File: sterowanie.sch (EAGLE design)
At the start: 8 parts

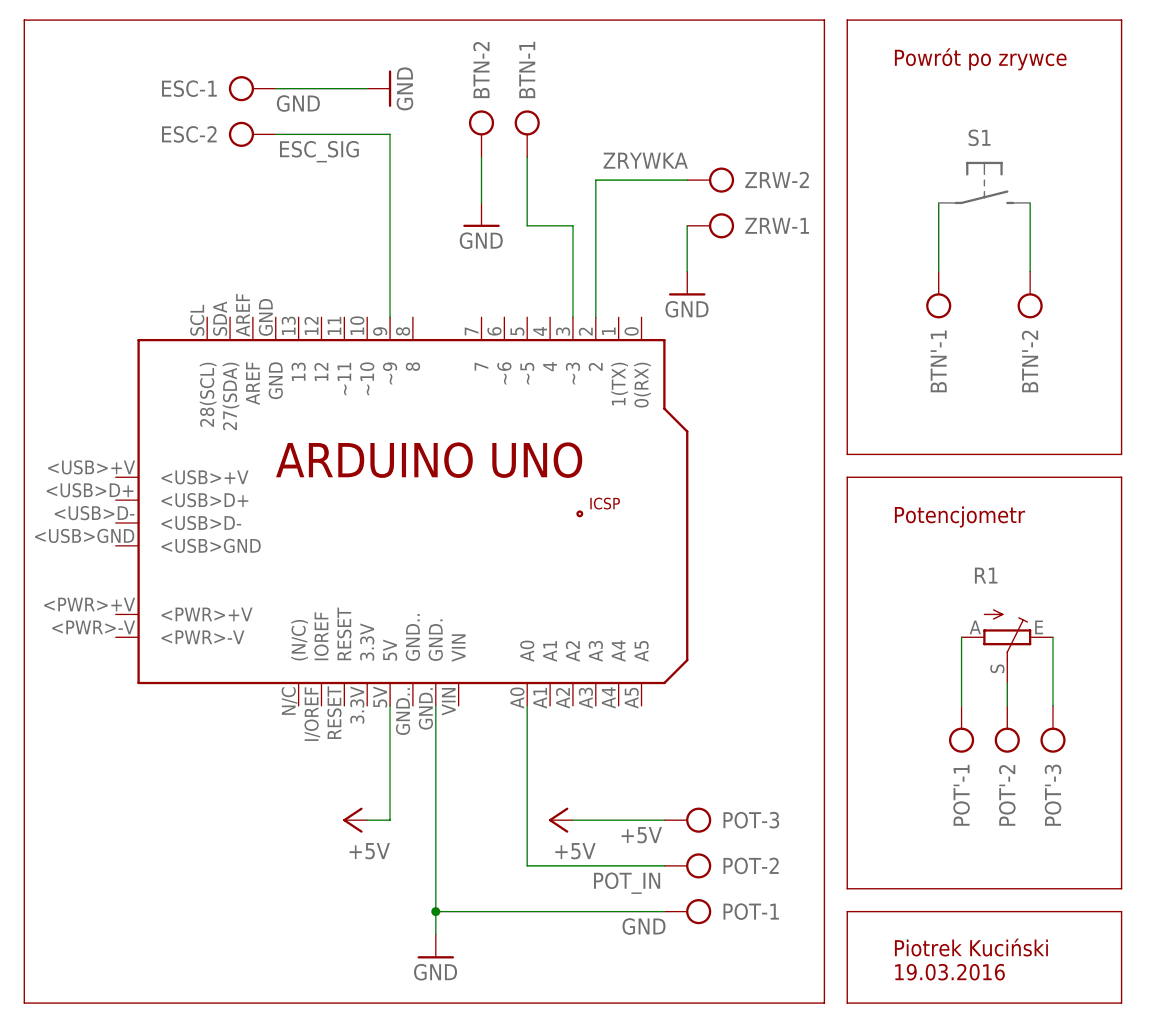
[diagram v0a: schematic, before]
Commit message: poprawiony schemat, dodane PCB jako shield do Arduino
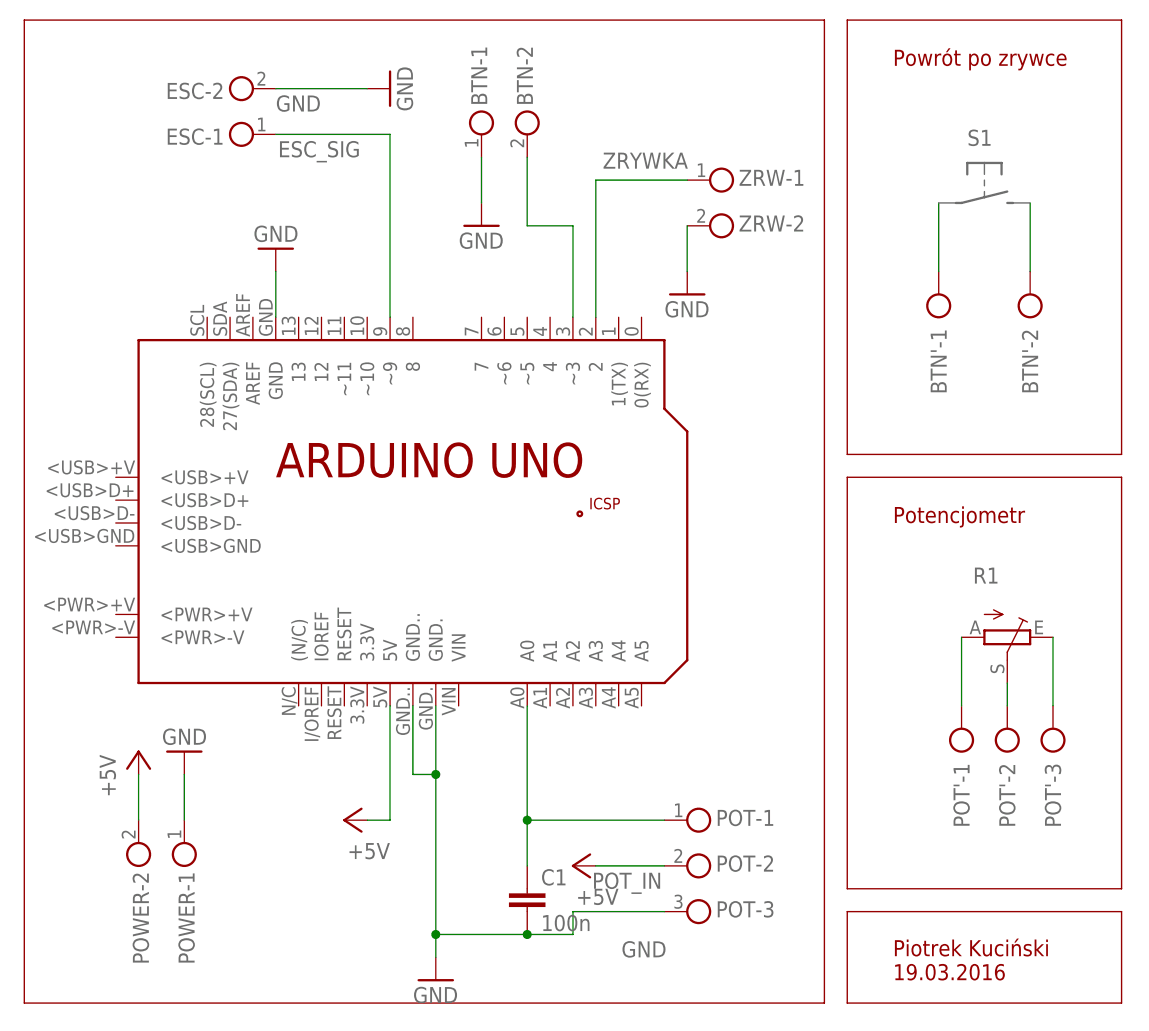
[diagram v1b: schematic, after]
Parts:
- added C1: 100n, rcl:C-EUC1206
- added POWER: (no value), con-ria-59:AKL59-02
- BTN, ESC, ZRW: device con-ptr500:AK300/2 -> con-ria-59:AKL59-02
- POT: device con-ptr500:AK300/3 -> con-ria-59:AKL59-03
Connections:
- net +5V: now also POT-2.1, POWER-2.1; no longer POT-3.KL
- net ESC_SIG: now also ESC-1.1; no longer ESC-2.KL
- net GND: now also BTN-1.1, C1.2, ESC-2.1, PCB1.GND, PCB1.GND.., POT-3.1, POWER-1.1, ZRW-2.1; no longer BTN-2.KL, ESC-1.KL, POT-1.KL, ZRW-1.KL
- net N$1: now also BTN-2.1; no longer BTN-1.KL
- net POT_IN: now also C1.1, POT-1.1; no longer POT-2.KL
- net ZRYWKA: now also ZRW-1.1; no longer ZRW-2.KL
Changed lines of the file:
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@@
 <part name="PCB1" library="E14_Arduino_revB" deviceset="ARDUINO_UNO" device=""/>
 <part name="S1" library="switch-omron" deviceset="D-TS" device=""/>
-<part name="ZRW" library="con-ptr500" deviceset="AK300/2" device=""/>
-<part name="POT" library="con-ptr500" deviceset="AK300/3" device=""/>
-<part name="ESC" library="con-ptr500" deviceset="AK300/2" device=""/>
 <part name="P+1" library="supply1" deviceset="+5V" device=""/>
 <part name="GND1" library="supply1" deviceset="GND" device=""/>
@@
 <part name="GND3" library="supply1" deviceset="GND" device=""/>
 <part name="GND4" library="supply1" deviceset="GND" device=""/>
-<part name="BTN" library="con-ptr500" deviceset="AK300/2" device=""/>
 <part name="BTN'" library="con-ptr500" deviceset="AK300/2" device=""/>
 <part name="POT'" library="con-ptr500" deviceset="AK300/3" device=""/>
 <part name="R1" library="pot" deviceset="TRIM_EU-" device="B90P"/>
+<part name="P+3" library="supply1" deviceset="+5V" device=""/>
+<part name="GND5" library="supply1" deviceset="GND" device=""/>
+<part name="C1" library="rcl" deviceset="C-EU" device="C1206" value="100n"/>
+<part name="POT" library="con-ria-59" deviceset="AKL59-03" device=""/>
+<part name="POWER" library="con-ria-59" deviceset="AKL59-02" device=""/>
+<part name="BTN" library="con-ria-59" deviceset="AKL59-02" device=""/>
+<part name="ESC" library="con-ria-59" deviceset="AKL59-02" device=""/>
+<part name="ZRW" library="con-ria-59" deviceset="AKL59-02" device=""/>
+<part name="GND6" library="supply1" deviceset="GND" device=""/>
 </parts>
 <sheets>
@@
 <instance part="PCB1" gate="G$1" x="76.2" y="43.18"/>
 <instance part="S1" gate="G$1" x="139.7" y="76.2" rot="R270"/>
-<instance part="ZRW" gate="-1" x="111.76" y="73.66" rot="R180"/>
-<instance part="ZRW" gate="-2" x="111.76" y="78.74" rot="R180"/>
-<instance part="POT" gate="-1" x="109.22" y="-2.54" rot="R180"/>
-<instance part="POT" gate="-2" x="109.22" y="2.54" rot="R180"/>
-<instance part="POT" gate="-3" x="109.22" y="7.62" rot="R180"/>
-<instance part="ESC" gate="-1" x="55.88" y="88.9" smashed="yes">
-<attribute name="NAME" x="54.61" y="89.789" size="1.778" layer="95" rot="R180"/>
-</instance>
-<instance part="ESC" gate="-2" x="55.88" y="83.82" smashed="yes">
-<attribute name="NAME" x="54.61" y="84.709" size="1.778" layer="95" rot="R180"/>
-<attribute name="VALUE" x="52.07" y="80.137" size="1.778" layer="96"/>
-</instance>
 <instance part="P+1" gate="1" x="68.58" y="7.62" rot="R90"/>
-<instance part="GND1" gate="1" x="78.74" y="-7.62"/>
-<instance part="P+2" gate="1" x="91.44" y="7.62" rot="R90"/>
+<instance part="GND1" gate="1" x="78.74" y="-10.16"/>
+<instance part="P+2" gate="1" x="93.98" y="2.54" rot="R90"/>
 <instance part="GND2" gate="1" x="73.66" y="88.9" rot="R90"/>
 <instance part="GND3" gate="1" x="106.68" y="66.04"/>
 <instance part="GND4" gate="1" x="83.82" y="73.66"/>
-<instance part="BTN" gate="-1" x="88.9" y="86.36" rot="R270"/>
-<instance part="BTN" gate="-2" x="83.82" y="86.36" rot="R270"/>
 <instance part="BTN'" gate="-1" x="134.62" y="63.5" rot="R90"/>
 <instance part="BTN'" gate="-2" x="144.78" y="63.5" rot="R90"/>
@@
 <instance part="POT'" gate="-3" x="147.32" y="15.24" rot="R90"/>
 <instance part="R1" gate="1" x="142.24" y="27.94" rot="R270"/>
+<instance part="P+3" gate="1" x="45.72" y="15.24"/>
+<instance part="GND5" gate="1" x="50.8" y="15.24" rot="R180"/>
+<instance part="C1" gate="G$1" x="88.9" y="0"/>
+<instance part="POT" gate="-1" x="104.14" y="7.62"/>
+<instance part="POT" gate="-2" x="104.14" y="2.54"/>
+<instance part="POT" gate="-3" x="104.14" y="-2.54"/>
+<instance part="POWER" gate="-1" x="50.8" y="7.62" rot="R270"/>
+<instance part="POWER" gate="-2" x="45.72" y="7.62" rot="R270"/>
+<instance part="BTN" gate="-1" x="83.82" y="81.28" rot="R90"/>
+<instance part="BTN" gate="-2" x="88.9" y="81.28" rot="R90"/>
+<instance part="ESC" gate="-1" x="60.96" y="83.82" rot="R180"/>
+<instance part="ESC" gate="-2" x="60.96" y="88.9" rot="R180"/>
+<instance part="ZRW" gate="-1" x="106.68" y="78.74"/>
+<instance part="ZRW" gate="-2" x="106.68" y="73.66"/>
+<instance part="GND6" gate="1" x="60.96" y="71.12" rot="R180"/>
 </instances>
 <busses>
@@
 </segment>
 <segment>
-<pinref part="POT" gate="-3" pin="KL"/>
+<pinref part="P+3" gate="1" pin="+5V"/>
+<wire x1="45.72" y1="7.62" x2="45.72" y2="12.7" width="0.1524" layer="91"/>
+<pinref part="POWER" gate="-2" pin="1"/>
+</segment>
+<segment>
 <pinref part="P+2" gate="1" pin="+5V"/>
-<wire x1="93.98" y1="7.62" x2="104.14" y2="7.62" width="0.1524" layer="91"/>
-<label x="103.886" y="6.858" size="1.778" layer="95" rot="R180"/>
+<pinref part="POT" gate="-2" pin="1"/>
+<wire x1="96.52" y1="2.54" x2="104.14" y2="2.54" width="0.1524" layer="91"/>
 </segment>
 </net>
@@
 <pinref part="PCB1" gate="G$1" pin="GND."/>
 <pinref part="GND1" gate="1" pin="GND"/>
-<wire x1="78.74" y1="20.32" x2="78.74" y2="-2.54" width="0.1524" layer="91"/>
-<pinref part="POT" gate="-1" pin="KL"/>
-<wire x1="78.74" y1="-2.54" x2="78.74" y2="-5.08" width="0.1524" layer="91"/>
-<wire x1="104.14" y1="-2.54" x2="78.74" y2="-2.54" width="0.1524" layer="91"/>
-<junction x="78.74" y="-2.54"/>
-<label x="104.394" y="-3.302" size="1.778" layer="95" rot="R180"/>
+<wire x1="78.74" y1="20.32" x2="78.74" y2="12.7" width="0.1524" layer="91"/>
+<wire x1="78.74" y1="12.7" x2="78.74" y2="-5.08" width="0.1524" layer="91"/>
+<wire x1="78.74" y1="-5.08" x2="78.74" y2="-7.62" width="0.1524" layer="91"/>
+<junction x="78.74" y="-5.08"/>
+<label x="104.394" y="-5.842" size="1.778" layer="95" rot="R180"/>
+<pinref part="C1" gate="G$1" pin="2"/>
+<wire x1="88.9" y1="-5.08" x2="78.74" y2="-5.08" width="0.1524" layer="91"/>
+<wire x1="104.14" y1="-2.54" x2="93.98" y2="-2.54" width="0.1524" layer="91"/>
+<wire x1="93.98" y1="-2.54" x2="93.98" y2="-5.08" width="0.1524" layer="91"/>
+<wire x1="93.98" y1="-5.08" x2="88.9" y2="-5.08" width="0.1524" layer="91"/>
+<junction x="88.9" y="-5.08"/>
+<pinref part="POT" gate="-3" pin="1"/>
+<pinref part="PCB1" gate="G$1" pin="GND.."/>
+<wire x1="76.2" y1="20.32" x2="76.2" y2="12.7" width="0.1524" layer="91"/>
+<wire x1="76.2" y1="12.7" x2="78.74" y2="12.7" width="0.1524" layer="91"/>
+<junction x="78.74" y="12.7"/>
 </segment>
 <segment>
-<pinref part="ESC" gate="-1" pin="KL"/>
 <pinref part="GND2" gate="1" pin="GND"/>
 <wire x1="60.96" y1="88.9" x2="71.12" y2="88.9" width="0.1524" layer="91"/>
 <label x="60.96" y="86.36" size="1.778" layer="95"/>
+<pinref part="ESC" gate="-2" pin="1"/>
 </segment>
 <segment>
-<pinref part="ZRW" gate="-1" pin="KL"/>
 <pinref part="GND3" gate="1" pin="GND"/>
 <wire x1="106.68" y1="73.66" x2="106.68" y2="68.58" width="0.1524" layer="91"/>
+<pinref part="ZRW" gate="-2" pin="1"/>
 </segment>
 <segment>
-<pinref part="BTN" gate="-2" pin="KL"/>
 <pinref part="GND4" gate="1" pin="GND"/>
 <wire x1="83.82" y1="81.28" x2="83.82" y2="76.2" width="0.1524" layer="91"/>
+<pinref part="BTN" gate="-1" pin="1"/>
+</segment>
+<segment>
+<pinref part="GND5" gate="1" pin="GND"/>
+<wire x1="50.8" y1="7.62" x2="50.8" y2="12.7" width="0.1524" layer="91"/>
+<pinref part="POWER" gate="-1" pin="1"/>
+</segment>
+<segment>
+<pinref part="PCB1" gate="G$1" pin="GND"/>
+<pinref part="GND6" gate="1" pin="GND"/>
+<wire x1="60.96" y1="68.58" x2="60.96" y2="63.5" width="0.1524" layer="91"/>
 </segment>
 </net>
 <net name="POT_IN" class="0">
 <segment>
-<pinref part="POT" gate="-2" pin="KL"/>
 <pinref part="PCB1" gate="G$1" pin="A0"/>
-<wire x1="104.14" y1="2.54" x2="88.9" y2="2.54" width="0.1524" layer="91"/>
-<wire x1="88.9" y1="2.54" x2="88.9" y2="20.32" width="0.1524" layer="91"/>
+<wire x1="88.9" y1="2.54" x2="88.9" y2="7.62" width="0.1524" layer="91"/>
 <label x="103.886" y="1.778" size="1.778" layer="95" rot="R180"/>
+<pinref part="C1" gate="G$1" pin="1"/>
+<pinref part="POT" gate="-1" pin="1"/>
+<wire x1="88.9" y1="7.62" x2="88.9" y2="20.32" width="0.1524" layer="91"/>
+<wire x1="104.14" y1="7.62" x2="88.9" y2="7.62" width="0.1524" layer="91"/>
+<junction x="88.9" y="7.62"/>
 </segment>
 </net>
 <net name="ESC_SIG" class="0">
 <segment>
-<pinref part="ESC" gate="-2" pin="KL"/>
 <pinref part="PCB1" gate="G$1" pin="~9"/>
 <wire x1="60.96" y1="83.82" x2="73.66" y2="83.82" width="0.1524" layer="91"/>
 <wire x1="73.66" y1="83.82" x2="73.66" y2="63.5" width="0.1524" layer="91"/>
 <label x="61.214" y="81.28" size="1.778" layer="95"/>
+<pinref part="ESC" gate="-1" pin="1"/>
 </segment>
 </net>
 <net name="ZRYWKA" class="0">
 <segment>
-<pinref part="ZRW" gate="-2" pin="KL"/>
 <pinref part="PCB1" gate="G$1" pin="2"/>
 <wire x1="106.68" y1="78.74" x2="96.52" y2="78.74" width="0.1524" layer="91"/>
 <wire x1="96.52" y1="78.74" x2="96.52" y2="63.5" width="0.1524" layer="91"/>
 <label x="97.282" y="80.01" size="1.778" layer="95"/>
+<pinref part="ZRW" gate="-1" pin="1"/>
 </segment>
 </net>
@@
 <pinref part="PCB1" gate="G$1" pin="~3"/>
 <wire x1="93.98" y1="63.5" x2="93.98" y2="73.66" width="0.1524" layer="91"/>
-<pinref part="BTN" gate="-1" pin="KL"/>
 <wire x1="93.98" y1="73.66" x2="88.9" y2="73.66" width="0.1524" layer="91"/>
 <wire x1="88.9" y1="73.66" x2="88.9" y2="81.28" width="0.1524" layer="91"/>
+<pinref part="BTN" gate="-2" pin="1"/>
 </segment>
 </net>
